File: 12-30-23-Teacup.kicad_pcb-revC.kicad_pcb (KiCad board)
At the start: 4 copper layers, 86.2 x 56.2 mm, 100 parts, among them IC1 T31ZX, J1 USB Type-C, J10 AudioJack4_Ground, J11 Conn_01x04_Pin, J12 Conn_01x04_Pin, J13 SFW15R-2STE1LF, J2 Micro_SD_Card, J3 USB_A, J4 Conn_02x08_Odd_Even, J5 UART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

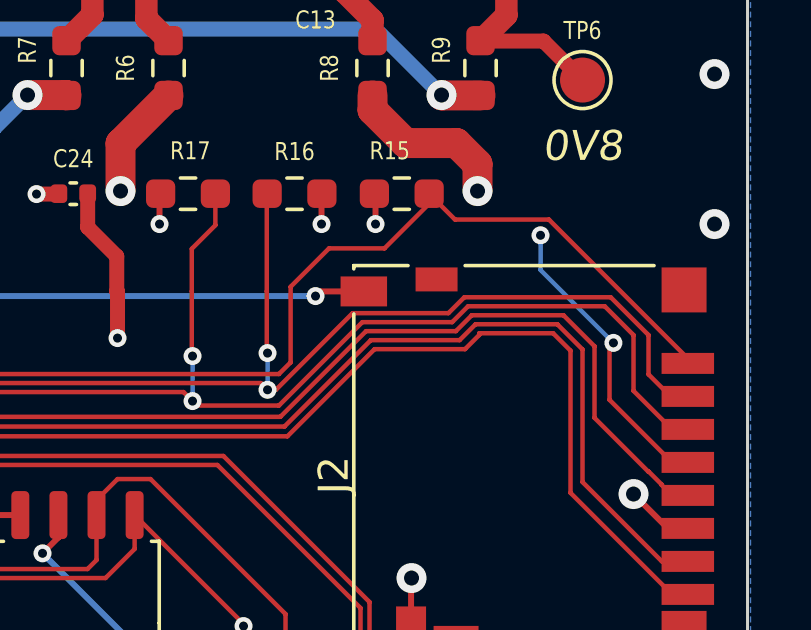
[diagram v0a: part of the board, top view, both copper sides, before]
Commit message: Added R22 pullup resistor on PB27 to help the card detect recognition on the SD card
Added R22 pullup resistor on PB27 to help the card detect recognition on the SD card
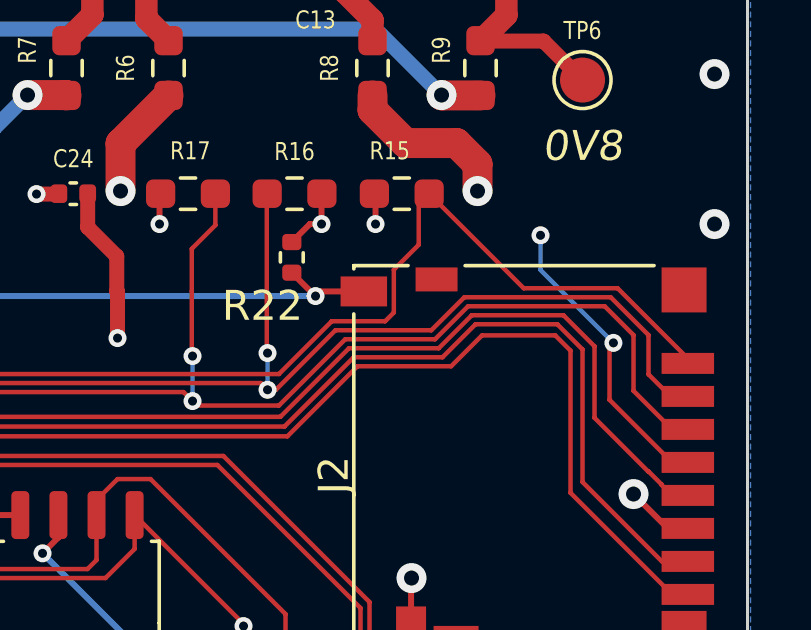
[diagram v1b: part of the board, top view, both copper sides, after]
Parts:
- added R22: 1M, Resistor_SMD:R_0402_1005Metric, F.Cu at (232.9, 76.1)
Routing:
- net +3V3: track 258.5 -> 259.7 mm
- net /PB27: track 102.5 -> 103.6 mm
